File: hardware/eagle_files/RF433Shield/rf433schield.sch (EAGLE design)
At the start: 3 parts, among them U1 ARDUINOR3-DIMENSION

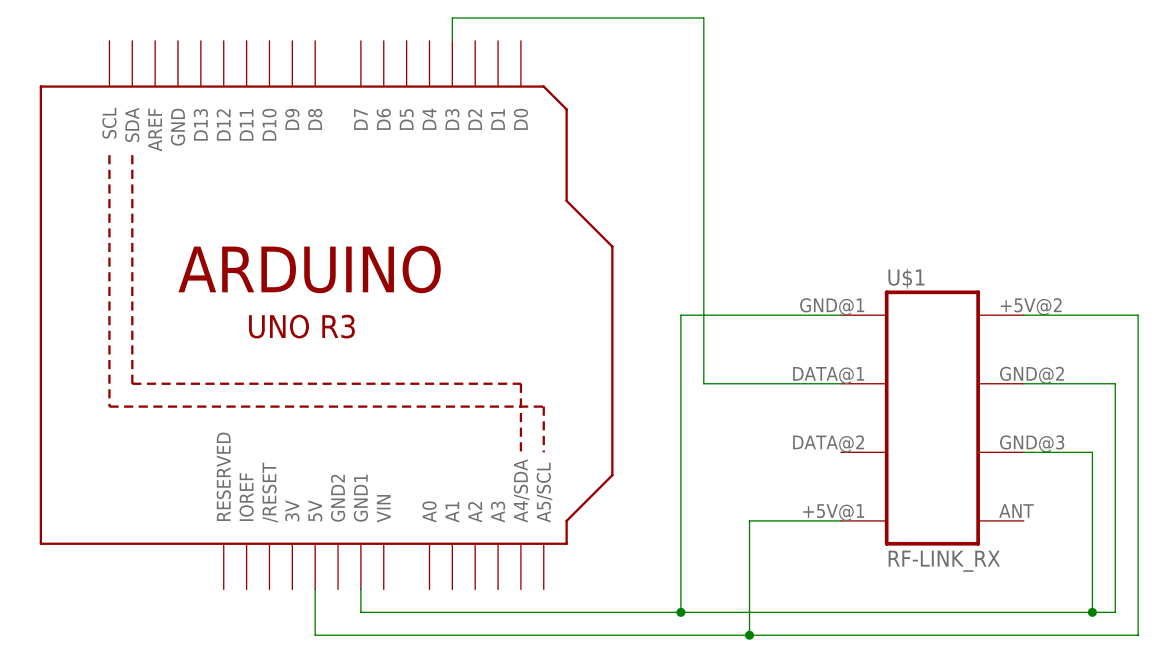
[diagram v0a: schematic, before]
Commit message: Added ICeePot logo on the copper of the board
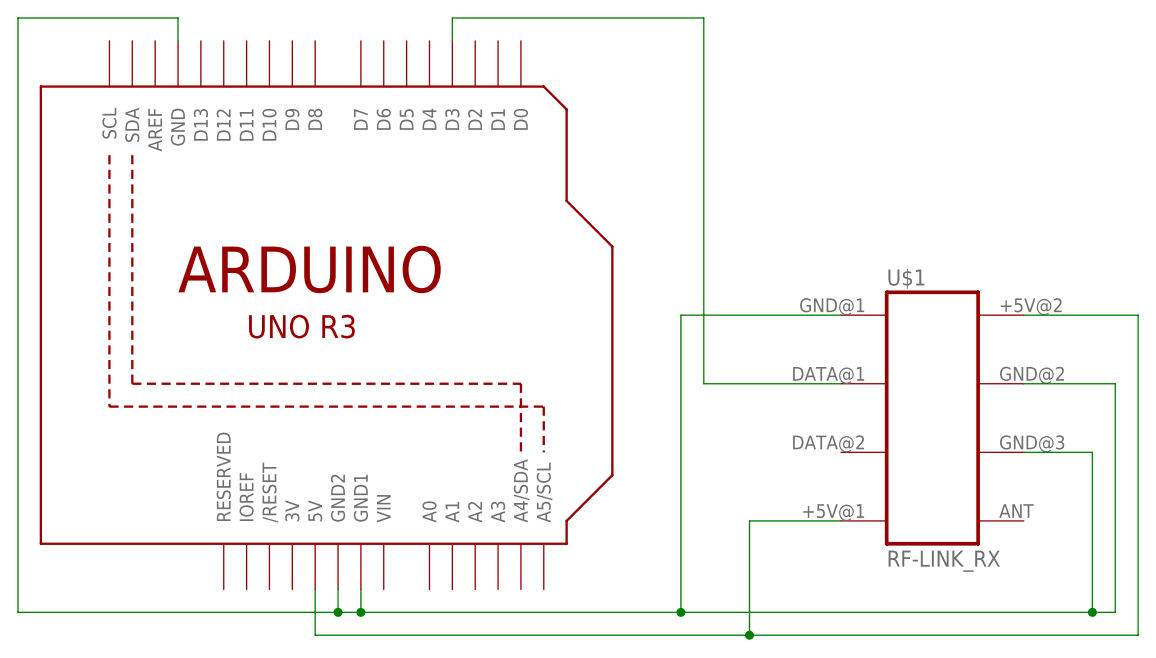
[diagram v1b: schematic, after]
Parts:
- removed U$2: ICEEPOT_LOGO, RFM:ICEEPOT_LOGO
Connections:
- net N$2 renamed VCC
- removed net N$3: U$1.GND1, U$1.GND2, U$1.GND3, U1.GND1
- new net GND: U$1.GND1, U$1.GND2, U$1.GND3, U1.GND, U1.GND1, U1.GND2
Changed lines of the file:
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@@
 <part name="U$1" library="RFM" deviceset="RF-LINK_RX" device=""/>
 <part name="U1" library="RFM" deviceset="ARDUINOR3" device="-DIMENSION"/>
-<part name="U$2" library="RFM" deviceset="ICEEPOT_LOGO" device=""/>
 </parts>
 <sheets>
@@
 <instance part="U$1" gate="G$1" x="91.44" y="43.18"/>
 <instance part="U1" gate="G$1" x="25.4" y="53.34"/>
-<instance part="U$2" gate="G$1" x="76.2" y="63.5"/>
 </instances>
 <busses>
@@
 </segment>
 </net>
-<net name="N$2" class="0">
+<net name="VCC" class="0">
 <segment>
 <wire x1="22.86" y1="22.86" x2="22.86" y2="17.78" width="0.1524" layer="91"/>
@@
 </segment>
 </net>
-<net name="N$3" class="0">
+<net name="GND" class="0">
 <segment>
 <wire x1="63.5" y1="20.32" x2="63.5" y2="53.34" width="0.1524" layer="91"/>
@@
 <pinref part="U$1" gate="G$1" pin="GND3"/>
 <pinref part="U1" gate="G$1" pin="GND1"/>
+<wire x1="-10.16" y1="86.36" x2="-10.16" y2="20.32" width="0.1524" layer="91"/>
+<pinref part="U1" gate="G$1" pin="GND2"/>
+<wire x1="-10.16" y1="20.32" x2="25.4" y2="20.32" width="0.1524" layer="91"/>
+<wire x1="25.4" y1="22.86" x2="25.4" y2="20.32" width="0.1524" layer="91"/>
+<wire x1="25.4" y1="20.32" x2="27.94" y2="20.32" width="0.1524" layer="91"/>
+<junction x="25.4" y="20.32"/>
+<junction x="27.94" y="20.32"/>
+<pinref part="U1" gate="G$1" pin="GND"/>
+<wire x1="7.62" y1="83.82" x2="7.62" y2="86.36" width="0.1524" layer="91"/>
+<wire x1="-10.16" y1="86.36" x2="7.62" y2="86.36" width="0.1524" layer="91"/>
 </segment>
 </net>
@@
 </sheet>
 </sheets>
-<errors>
-</errors>
 </schematic>
 </drawing>
